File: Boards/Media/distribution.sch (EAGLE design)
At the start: 16 parts

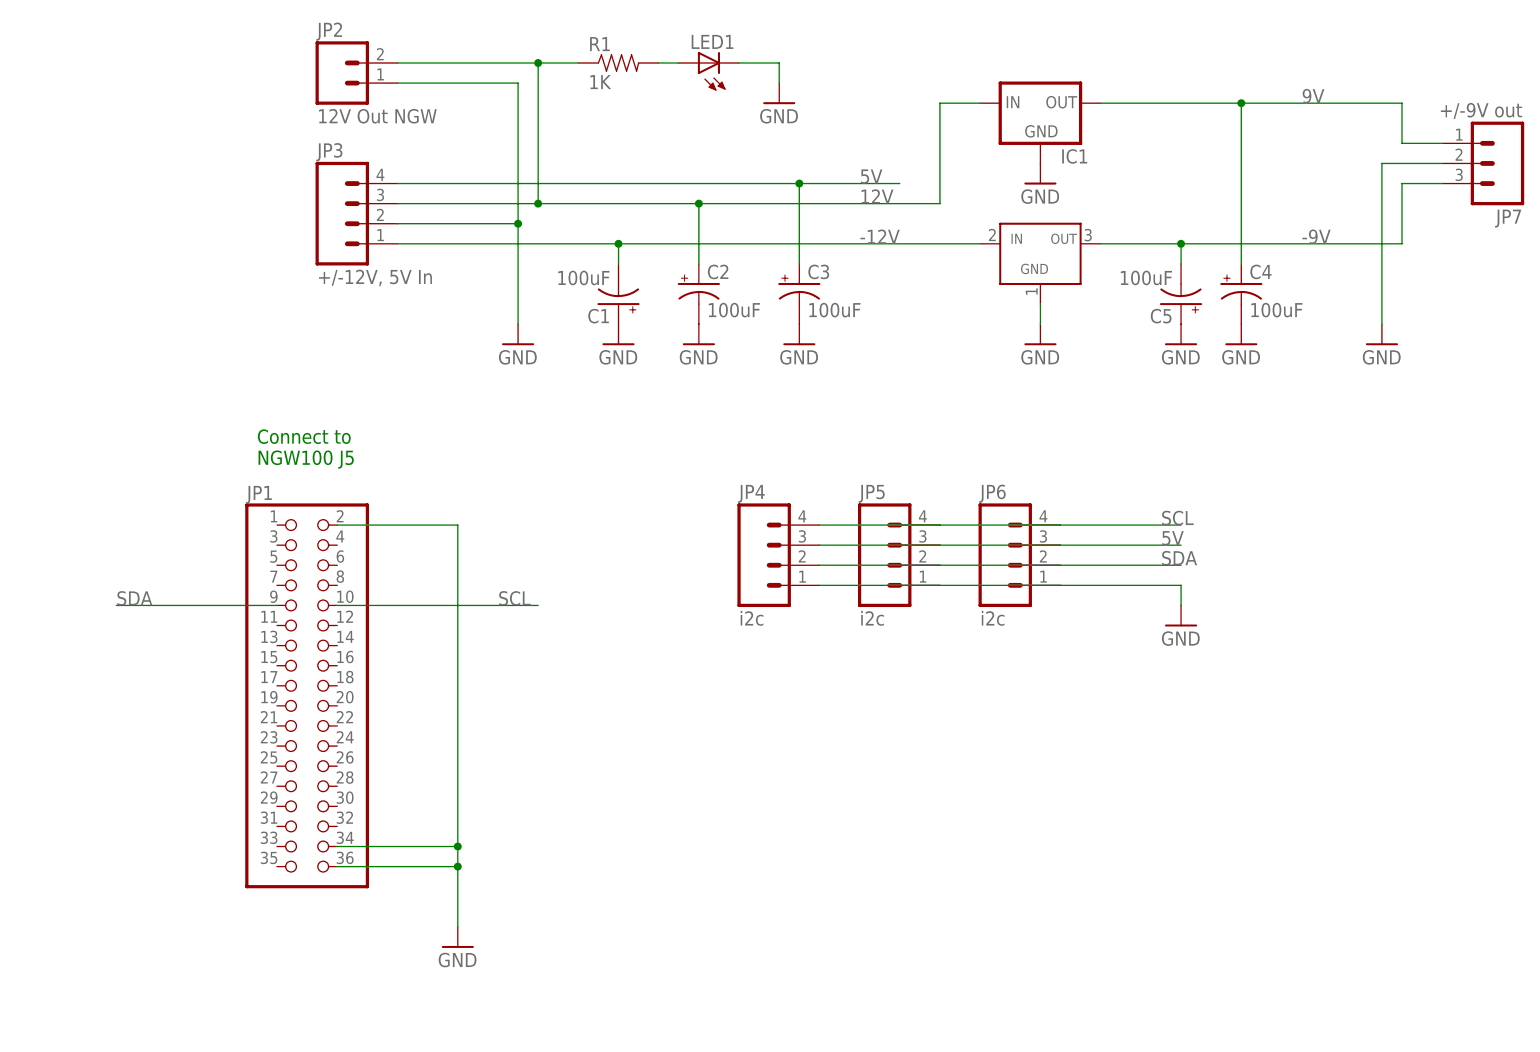
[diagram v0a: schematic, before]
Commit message: Changed to a PI GPIO header (ditching the NGW100)
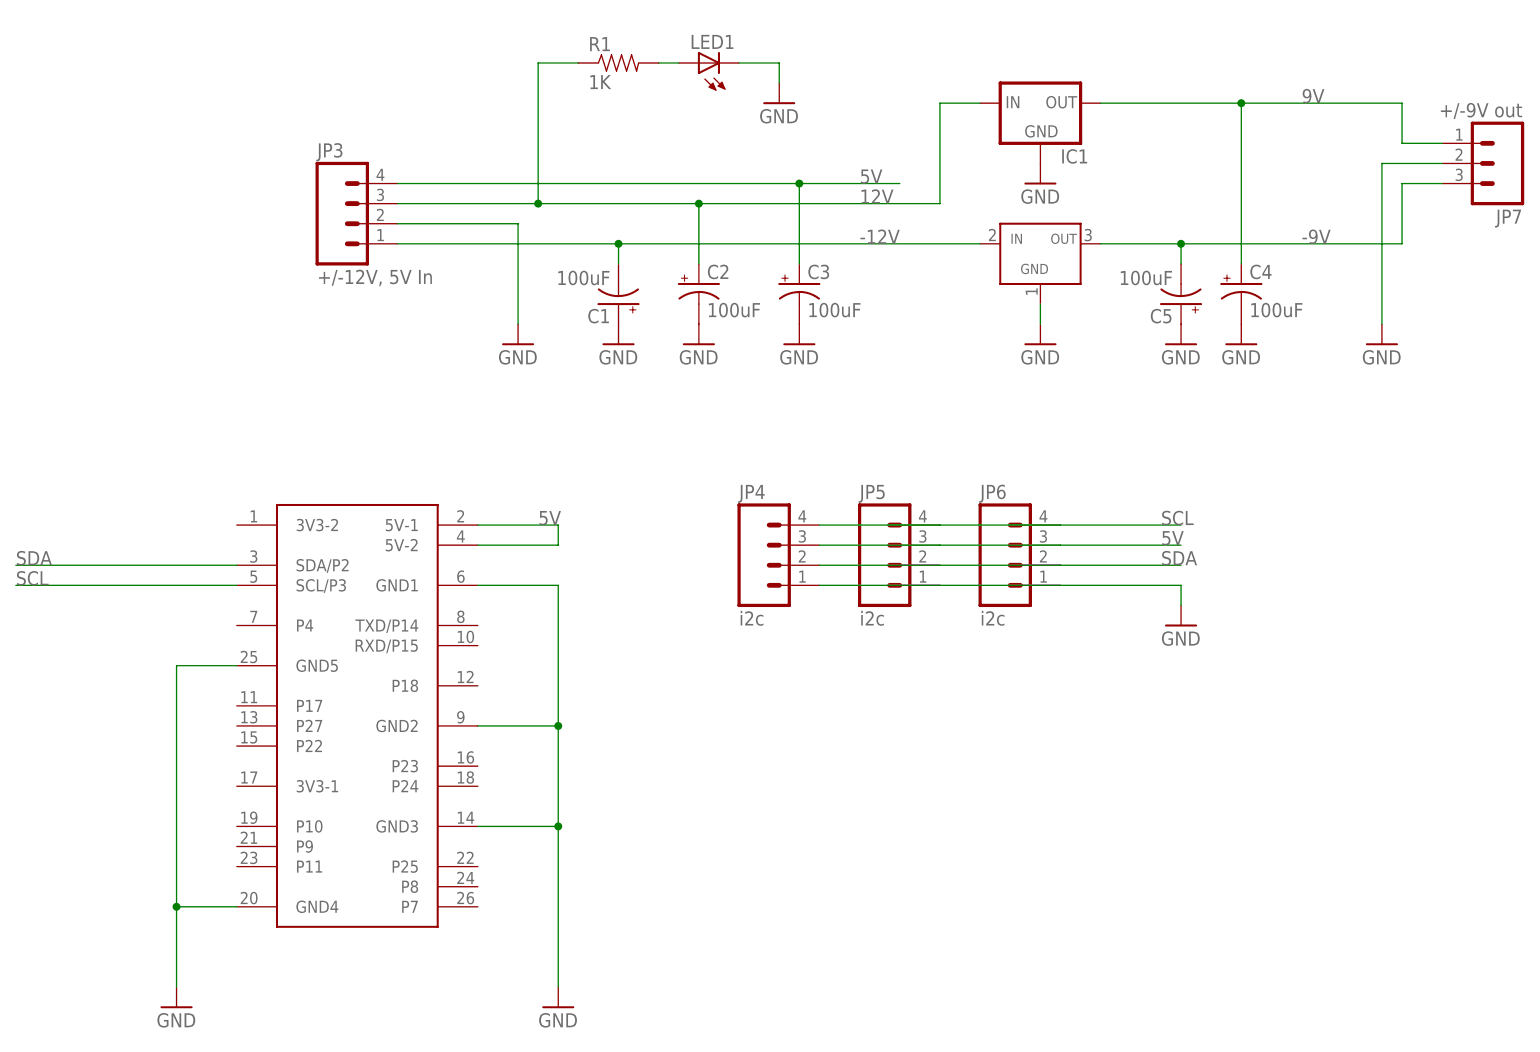
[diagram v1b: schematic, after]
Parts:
- removed JP1: (no value), pinhead:PINHD-2X18
- removed JP2: 12V Out NGW, 1_SparkFun-Connectors:M023.5MM
- added U$2: PI-GPIO, 0_Tristan's_Lib:PI-GPIO
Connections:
- net 12V: no longer JP2.2
- net 5V: now also U$2.5V-1, U$2.5V-2
- net GND: now also U$2.GND1, U$2.GND2, U$2.GND3, U$2.GND4, U$2.GND5; no longer JP1.2, JP1.34, JP1.36, JP2.1
- net SCL: now also U$2.SCL/P3; no longer JP1.10
- net SDA: now also U$2.SDA/P2; no longer JP1.9
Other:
- note removed: "Connect to NGW100 J5"
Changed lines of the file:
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@@
 <?xml version="1.0" encoding="utf-8"?>
 <!DOCTYPE eagle SYSTEM "eagle.dtd">
-<eagle version="7.1.0">
+<eagle version="6.6.0">
 <drawing>
 <settings>
@@
 <layers>
 <layer number="1" name="Top" color="4" fill="1" visible="no" active="no"/>
+<layer number="2" name="Route2" color="1" fill="3" visible="no" active="no"/>
+<layer number="3" name="Route3" color="4" fill="3" visible="no" active="no"/>
+<layer number="14" name="Route14" color="1" fill="6" visible="no" active="no"/>
+<layer number="15" name="Route15" color="4" fill="6" visible="no" active="no"/>
 <layer number="16" name="Bottom" color="1" fill="1" visible="no" active="no"/>
 <layer number="17" name="Pads" color="2" fill="1" visible="no" active="no"/>
@@
 <parts>
 <part name="FRAME1" library="1_SparkFun-Aesthetics" deviceset="FRAME-A3" device=""/>
-<part name="JP1" library="pinhead" deviceset="PINHD-2X18" device=""/>
-<part name="GND1" library="1_SparkFun-Aesthetics" deviceset="GND" device=""/>
-<part name="JP2" library="1_SparkFun-Connectors" deviceset="M02" device="3.5MM" value="12V Out NGW"/>
 <part name="GND2" library="1_SparkFun-Aesthetics" deviceset="GND" device=""/>
 <part name="GND3" library="1_SparkFun-Aesthetics" deviceset="GND" device=""/>
@@
 <part name="JP7" library="1_SparkFun-Connectors" deviceset="M03" device="POLAR" value="+/-9V out"/>
 <part name="GND12" library="1_SparkFun-Aesthetics" deviceset="GND" device=""/>
+<part name="U$2" library="0_Tristan's_Lib" deviceset="PI-GPIO" device=""/>
+<part name="GND1" library="1_SparkFun-Aesthetics" deviceset="GND" device=""/>
+<part name="GND13" library="1_SparkFun-Aesthetics" deviceset="GND" device=""/>
 </parts>
 <sheets>
 <sheet>
 <plain>
-<text x="58.42" y="124.46" size="1.778" layer="91">Connect to
-NGW100 J5</text>
 </plain>
 <instances>
 <instance part="FRAME1" gate="G$1" x="0" y="0"/>
-<instance part="JP1" gate="A" x="63.5" y="96.52"/>
-<instance part="GND1" gate="1" x="83.82" y="63.5"/>
-<instance part="JP2" gate="G$1" x="68.58" y="172.72"/>
 <instance part="GND2" gate="1" x="91.44" y="139.7"/>
 <instance part="GND3" gate="1" x="104.14" y="139.7"/>
@@
 <instance part="JP7" gate="G$1" x="215.9" y="162.56" rot="R180"/>
 <instance part="GND12" gate="1" x="200.66" y="139.7"/>
+<instance part="U$2" gate="G$1" x="71.12" y="91.44"/>
+<instance part="GND1" gate="1" x="48.26" y="55.88"/>
+<instance part="GND13" gate="1" x="96.52" y="55.88"/>
 </instances>
 <busses>
@@
 <net name="GND" class="0">
 <segment>
-<pinref part="JP1" gate="A" pin="2"/>
-<wire x1="68.58" y1="116.84" x2="83.82" y2="116.84" width="0.1524" layer="91"/>
-<wire x1="83.82" y1="116.84" x2="83.82" y2="76.2" width="0.1524" layer="91"/>
-<pinref part="JP1" gate="A" pin="34"/>
-<wire x1="83.82" y1="76.2" x2="83.82" y2="73.66" width="0.1524" layer="91"/>
-<wire x1="83.82" y1="73.66" x2="83.82" y2="66.04" width="0.1524" layer="91"/>
-<wire x1="68.58" y1="76.2" x2="83.82" y2="76.2" width="0.1524" layer="91"/>
-<pinref part="JP1" gate="A" pin="36"/>
-<wire x1="68.58" y1="73.66" x2="83.82" y2="73.66" width="0.1524" layer="91"/>
-<junction x="83.82" y="76.2"/>
-<junction x="83.82" y="73.66"/>
-<pinref part="GND1" gate="1" pin="GND"/>
-</segment>
-<segment>
 <wire x1="76.2" y1="154.94" x2="91.44" y2="154.94" width="0.1524" layer="91"/>
 <wire x1="91.44" y1="154.94" x2="91.44" y2="142.24" width="0.1524" layer="91"/>
-<pinref part="JP2" gate="G$1" pin="1"/>
-<wire x1="76.2" y1="172.72" x2="91.44" y2="172.72" width="0.1524" layer="91"/>
-<wire x1="91.44" y1="172.72" x2="91.44" y2="154.94" width="0.1524" layer="91"/>
 <pinref part="GND2" gate="1" pin="GND"/>
-<junction x="91.44" y="154.94"/>
 <pinref part="JP3" gate="G$1" pin="2"/>
 </segment>
@@
 <pinref part="GND12" gate="1" pin="GND"/>
 </segment>
+<segment>
+<pinref part="U$2" gate="G$1" pin="GND5"/>
+<wire x1="55.88" y1="99.06" x2="48.26" y2="99.06" width="0.1524" layer="91"/>
+<wire x1="48.26" y1="99.06" x2="48.26" y2="68.58" width="0.1524" layer="91"/>
+<pinref part="U$2" gate="G$1" pin="GND4"/>
+<wire x1="48.26" y1="68.58" x2="48.26" y2="58.42" width="0.1524" layer="91"/>
+<wire x1="55.88" y1="68.58" x2="48.26" y2="68.58" width="0.1524" layer="91"/>
+<pinref part="GND1" gate="1" pin="GND"/>
+<junction x="48.26" y="68.58"/>
+</segment>
+<segment>
+<pinref part="U$2" gate="G$1" pin="GND1"/>
+<wire x1="86.36" y1="109.22" x2="96.52" y2="109.22" width="0.1524" layer="91"/>
+<wire x1="96.52" y1="109.22" x2="96.52" y2="91.44" width="0.1524" layer="91"/>
+<pinref part="U$2" gate="G$1" pin="GND3"/>
+<wire x1="96.52" y1="91.44" x2="96.52" y2="78.74" width="0.1524" layer="91"/>
+<wire x1="96.52" y1="78.74" x2="96.52" y2="58.42" width="0.1524" layer="91"/>
+<wire x1="86.36" y1="78.74" x2="96.52" y2="78.74" width="0.1524" layer="91"/>
+<pinref part="U$2" gate="G$1" pin="GND2"/>
+<wire x1="86.36" y1="91.44" x2="96.52" y2="91.44" width="0.1524" layer="91"/>
+<pinref part="GND13" gate="1" pin="GND"/>
+<junction x="96.52" y="91.44"/>
+<junction x="96.52" y="78.74"/>
+</segment>
 </net>
 <net name="SCL" class="0">
-<segment>
-<pinref part="JP1" gate="A" pin="10"/>
-<wire x1="68.58" y1="106.68" x2="93.98" y2="106.68" width="0.1524" layer="91"/>
-<label x="88.9" y="106.68" size="1.778" layer="95"/>
-</segment>
 <segment>
 <pinref part="JP4" gate="G$1" pin="4"/>
@@
 <label x="172.72" y="116.84" size="1.778" layer="95"/>
 </segment>
+<segment>
+<pinref part="U$2" gate="G$1" pin="SCL/P3"/>
+<wire x1="55.88" y1="109.22" x2="27.94" y2="109.22" width="0.1524" layer="91"/>
+<label x="27.94" y="109.22" size="1.778" layer="95"/>
+</segment>
 </net>
 <net name="SDA" class="0">
-<segment>
-<pinref part="JP1" gate="A" pin="9"/>
-<wire x1="60.96" y1="106.68" x2="40.64" y2="106.68" width="0.1524" layer="91"/>
-<label x="40.64" y="106.68" size="1.778" layer="95"/>
-</segment>
 <segment>
 <pinref part="JP4" gate="G$1" pin="2"/>
@@
 <label x="172.72" y="111.76" size="1.778" layer="95"/>
 </segment>
+<segment>
+<pinref part="U$2" gate="G$1" pin="SDA/P2"/>
+<wire x1="55.88" y1="111.76" x2="27.94" y2="111.76" width="0.1524" layer="91"/>
+<label x="27.94" y="111.76" size="1.778" layer="95"/>
+</segment>
 </net>
 <net name="12V" class="0">
@@
 <wire x1="76.2" y1="157.48" x2="93.98" y2="157.48" width="0.1524" layer="91"/>
 <wire x1="93.98" y1="157.48" x2="93.98" y2="175.26" width="0.1524" layer="91"/>
-<pinref part="JP2" gate="G$1" pin="2"/>
-<wire x1="93.98" y1="175.26" x2="76.2" y2="175.26" width="0.1524" layer="91"/>
 <wire x1="93.98" y1="157.48" x2="114.3" y2="157.48" width="0.1524" layer="91"/>
 <label x="134.62" y="157.48" size="1.778" layer="95"/>
@@
 <pinref part="R1" gate="G$1" pin="1"/>
 <wire x1="93.98" y1="175.26" x2="99.06" y2="175.26" width="0.1524" layer="91"/>
-<junction x="93.98" y="175.26"/>
 <wire x1="144.78" y1="157.48" x2="114.3" y2="157.48" width="0.1524" layer="91"/>
 <pinref part="JP3" gate="G$1" pin="3"/>
@@
 <wire x1="160.02" y1="114.3" x2="175.26" y2="114.3" width="0.1524" layer="91"/>
 <label x="172.72" y="114.3" size="1.778" layer="95"/>
+</segment>
+<segment>
+<pinref part="U$2" gate="G$1" pin="5V-2"/>
+<wire x1="86.36" y1="114.3" x2="96.52" y2="114.3" width="0.1524" layer="91"/>
+<wire x1="96.52" y1="114.3" x2="96.52" y2="116.84" width="0.1524" layer="91"/>
+<pinref part="U$2" gate="G$1" pin="5V-1"/>
+<wire x1="96.52" y1="116.84" x2="86.36" y2="116.84" width="0.1524" layer="91"/>
+<label x="93.98" y="116.84" size="1.778" layer="95"/>
 </segment>
 </net>
@@
 </schematic>
 </drawing>
-<compatibility>
-<note version="6.3" minversion="6.2.2" severity="warning">
-Since Version 6.2.2 text objects can contain more than one line,
-which will not be processed correctly with this version.
-</note>
-</compatibility>
 </eagle>

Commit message: Prepared board for production, last minute error checks and rotations
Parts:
- added JP1: UART, 1_SparkFun-Connectors:M03POLAR
- added R2, R3, R4, R5: 2k2, 1_SparkFun-Resistors:RESISTOR1206
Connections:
- new net N$2: R2.2, R3.2, U$2.3V3-2
- new net N$3: R4.2, U$2.TXD/P14
- new net N$4: R5.1, U$2.RXD/P15
- new net N$5: JP1.1, R4.1
- new net N$6: JP1.3, R5.2
- net GND: now also JP1.2
- net SCL: now also R3.1
- net SDA: now also R2.1
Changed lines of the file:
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@@
 <part name="GND1" library="1_SparkFun-Aesthetics" deviceset="GND" device=""/>
 <part name="GND13" library="1_SparkFun-Aesthetics" deviceset="GND" device=""/>
+<part name="JP1" library="1_SparkFun-Connectors" deviceset="M03" device="POLAR" value="UART"/>
+<part name="GND14" library="1_SparkFun-Aesthetics" deviceset="GND" device=""/>
+<part name="R2" library="1_SparkFun-Resistors" deviceset="RESISTOR" device="1206" value="2k2"/>
+<part name="R3" library="1_SparkFun-Resistors" deviceset="RESISTOR" device="1206" value="2k2"/>
+<part name="R4" library="1_SparkFun-Resistors" deviceset="RESISTOR" device="1206" value="2k2"/>
+<part name="R5" library="1_SparkFun-Resistors" deviceset="RESISTOR" device="1206" value="2k2"/>
 </parts>
 <sheets>
@@
 <instance part="GND1" gate="1" x="48.26" y="55.88"/>
 <instance part="GND13" gate="1" x="96.52" y="55.88"/>
+<instance part="JP1" gate="G$1" x="129.54" y="86.36" rot="R180"/>
+<instance part="GND14" gate="1" x="116.84" y="76.2"/>
+<instance part="R2" gate="G$1" x="40.64" y="121.92" rot="R90"/>
+<instance part="R3" gate="G$1" x="48.26" y="121.92" rot="R90"/>
+<instance part="R4" gate="G$1" x="104.14" y="104.14" rot="R180"/>
+<instance part="R5" gate="G$1" x="106.68" y="91.44" rot="R270"/>
 </instances>
 <busses>
@@
 <junction x="96.52" y="78.74"/>
 </segment>
+<segment>
+<pinref part="JP1" gate="G$1" pin="2"/>
+<wire x1="121.92" y1="86.36" x2="116.84" y2="86.36" width="0.1524" layer="91"/>
+<wire x1="116.84" y1="86.36" x2="116.84" y2="78.74" width="0.1524" layer="91"/>
+<pinref part="GND14" gate="1" pin="GND"/>
+</segment>
 </net>
 <net name="SCL" class="0">
@@
 <segment>
 <pinref part="U$2" gate="G$1" pin="SCL/P3"/>
-<wire x1="55.88" y1="109.22" x2="27.94" y2="109.22" width="0.1524" layer="91"/>
+<wire x1="55.88" y1="109.22" x2="48.26" y2="109.22" width="0.1524" layer="91"/>
 <label x="27.94" y="109.22" size="1.778" layer="95"/>
+<pinref part="R3" gate="G$1" pin="1"/>
+<wire x1="48.26" y1="109.22" x2="27.94" y2="109.22" width="0.1524" layer="91"/>
+<wire x1="48.26" y1="116.84" x2="48.26" y2="109.22" width="0.1524" layer="91"/>
+<junction x="48.26" y="109.22"/>
 </segment>
 </net>
@@
 <segment>
 <pinref part="U$2" gate="G$1" pin="SDA/P2"/>
-<wire x1="55.88" y1="111.76" x2="27.94" y2="111.76" width="0.1524" layer="91"/>
+<wire x1="55.88" y1="111.76" x2="40.64" y2="111.76" width="0.1524" layer="91"/>
 <label x="27.94" y="111.76" size="1.778" layer="95"/>
+<pinref part="R2" gate="G$1" pin="1"/>
+<wire x1="40.64" y1="111.76" x2="27.94" y2="111.76" width="0.1524" layer="91"/>
+<wire x1="40.64" y1="116.84" x2="40.64" y2="111.76" width="0.1524" layer="91"/>
+<junction x="40.64" y="111.76"/>
 </segment>
 </net>
@@
 </segment>
 </net>
+<net name="N$2" class="0">
+<segment>
+<pinref part="U$2" gate="G$1" pin="3V3-2"/>
+<wire x1="55.88" y1="116.84" x2="53.34" y2="116.84" width="0.1524" layer="91"/>
+<wire x1="53.34" y1="116.84" x2="53.34" y2="129.54" width="0.1524" layer="91"/>
+<pinref part="R2" gate="G$1" pin="2"/>
+<wire x1="53.34" y1="129.54" x2="48.26" y2="129.54" width="0.1524" layer="91"/>
+<wire x1="48.26" y1="129.54" x2="40.64" y2="129.54" width="0.1524" layer="91"/>
+<wire x1="40.64" y1="129.54" x2="40.64" y2="127" width="0.1524" layer="91"/>
+<pinref part="R3" gate="G$1" pin="2"/>
+<wire x1="48.26" y1="127" x2="48.26" y2="129.54" width="0.1524" layer="91"/>
+<junction x="48.26" y="129.54"/>
+</segment>
+</net>
+<net name="N$3" class="0">
+<segment>
+<pinref part="U$2" gate="G$1" pin="TXD/P14"/>
+<pinref part="R4" gate="G$1" pin="2"/>
+<wire x1="86.36" y1="104.14" x2="99.06" y2="104.14" width="0.1524" layer="91"/>
+</segment>
+</net>
+<net name="N$4" class="0">
+<segment>
+<pinref part="U$2" gate="G$1" pin="RXD/P15"/>
+<pinref part="R5" gate="G$1" pin="1"/>
+<wire x1="86.36" y1="101.6" x2="106.68" y2="101.6" width="0.1524" layer="91"/>
+<wire x1="106.68" y1="101.6" x2="106.68" y2="96.52" width="0.1524" layer="91"/>
+</segment>
+</net>
+<net name="N$5" class="0">
+<segment>
+<pinref part="R4" gate="G$1" pin="1"/>
+<wire x1="109.22" y1="104.14" x2="114.3" y2="104.14" width="0.1524" layer="91"/>
+<wire x1="114.3" y1="104.14" x2="114.3" y2="88.9" width="0.1524" layer="91"/>
+<pinref part="JP1" gate="G$1" pin="1"/>
+<wire x1="114.3" y1="88.9" x2="121.92" y2="88.9" width="0.1524" layer="91"/>
+</segment>
+</net>
+<net name="N$6" class="0">
+<segment>
+<pinref part="JP1" gate="G$1" pin="3"/>
+<pinref part="R5" gate="G$1" pin="2"/>
+<wire x1="121.92" y1="83.82" x2="106.68" y2="83.82" width="0.1524" layer="91"/>
+<wire x1="106.68" y1="83.82" x2="106.68" y2="86.36" width="0.1524" layer="91"/>
+</segment>
+</net>
